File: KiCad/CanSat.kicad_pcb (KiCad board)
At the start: 4 copper layers, 50 x 55 mm, 99 parts, among them J1 GPS, J10 LED, J11 PSU_CTRL, J12 POWER, J13 SWD, J14 SDCARD, J15 DF40C-100DS-0.4V(51), J16 DF40C-100DS-0.4V(51), J17 RPI_GPIO, J2 DEPLOY, J3 TEMP, J4 ENV_SENSORS, J5 RF_DATA, J6 GND, J7 GND, J9 COMM_ANT, P1 USB_SDR, U1 Ai-Thinker-Ra-01, U2 DS18B20U+, U3 STM32F407VGTx, U4 SN74LVC1G125DCKT, U5 USBLC6-2SC6, U6 SN74LVC1G125DCKT, Y1 16M

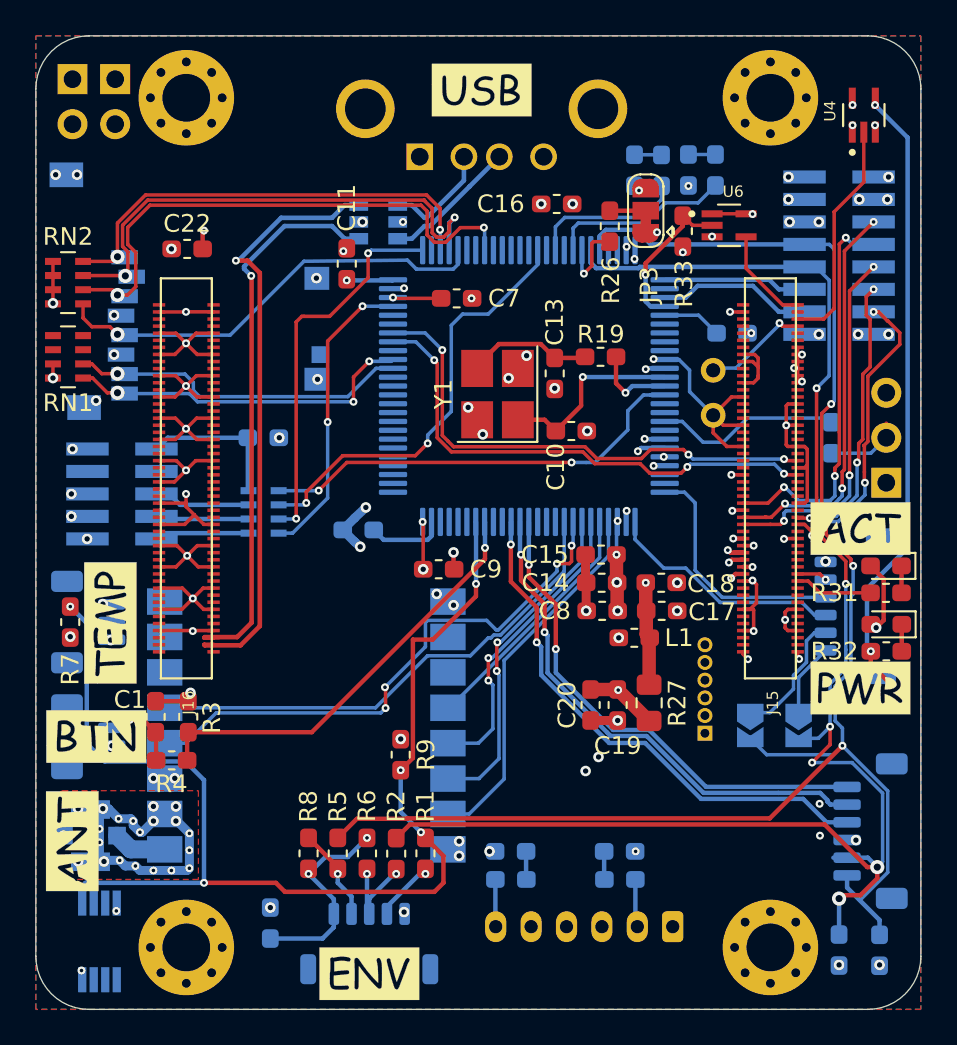
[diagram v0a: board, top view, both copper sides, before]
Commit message: Added a button and a buzzer
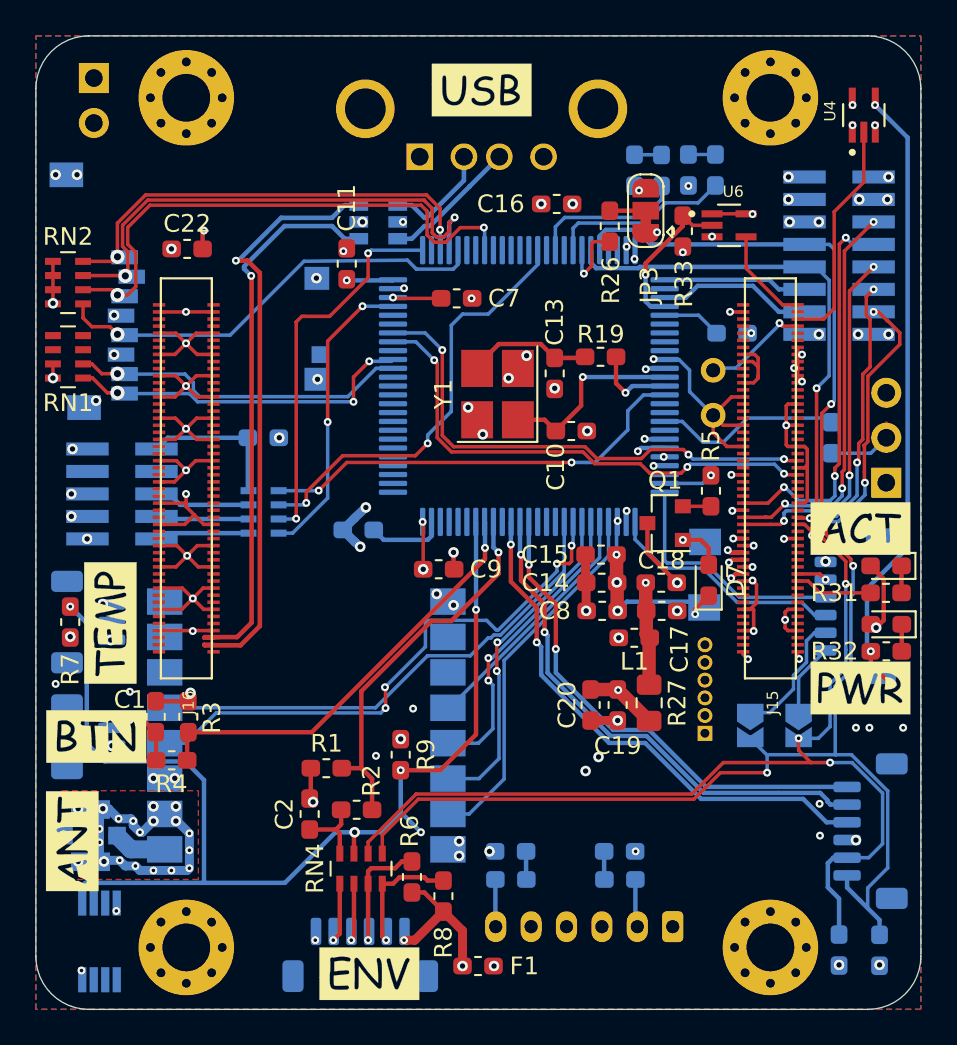
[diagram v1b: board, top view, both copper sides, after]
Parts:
- removed J7: GND, Connector_PinHeader_2.54mm:PinHeader_1x02_P2.54mm_Vertical
- added BZ1: Buzzer, Libs:MagneticBuzzer_INGHAi_GSC4417YA-16R4000, B.Cu at (222.8, 60.4)
- added C2: 1u, Capacitor_SMD:C_0603_1608Metric_Pad1.05x0.95mm_HandSolder, F.Cu at (200.5, 74.0)
- added D7: D_Small, Diode_SMD:D_0603_1608Metric_Pad1.05x0.95mm_HandSolder, F.Cu at (223.0, 60.8)
- added Q1: Q_NPN_CBE, Package_TO_SOT_SMD:SOT-23, F.Cu at (220.6, 57.5)
- added RN4: 22, Resistor_SMD:R_Array_Concave_4x0603, F.Cu at (203.4, 77.0)
- F1: moved to F.Cu
- J4: footprint Connector_JST:JST_SHL_SM05B-SHLS-TF_1x05-1MP_P1.00mm_Horizontal -> Connector_JST:JST_SH_BM06B-SRSS-TB_1x06-1MP_P1.00mm_Vertical
- R1: value 22 -> 10k
- R5: value 22 -> 1k
- moved R5 29.4 mm to (223.1, 55.7)
- moved F1 12.0 mm to (210.0, 82.5), turned to 0 degrees
- moved R8 7.99 mm to (208.0, 78.6)
- moved R1 7.38 mm to (201.4, 71.4), turned to 180 degrees
- moved R2 3.34 mm to (203.1, 73.7), turned to 0 degrees
- moved R6 2.87 mm to (206.2, 77.5), turned to 90 degrees
- moved J6 1.21 mm to (188.3, 32.4)
- moved J4 0.82 mm to (203.3, 81.9), turned to 0 degrees
- renumbered SCL to JP1, SDA to JP2, nBOOT to JP4
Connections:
- J4 pad 5: Net-(F1-Pad1) -> Net-(J4-Pad5)
- R1 pad 1: Net-(J4-Pad2) -> /Peripherals and Connectors/BUTTON
- R1 pad 2: /Peripherals and Connectors/DS_EXTERNAL -> GND
- R2 pad 1: Net-(J4-Pad3) -> Net-(C2-Pad1)
- R2 pad 2: /Peripherals and Connectors/SCL -> /Peripherals and Connectors/BUTTON
- R5 pad 1: Net-(J4-Pad4) -> Net-(Q1-Pad2)
- R5 pad 2: /Peripherals and Connectors/SDA -> /Peripherals and Connectors/BUZZER
- R6 pad 2: Net-(J4-Pad3) -> Net-(J4-Pad4)
- R8 pad 2: Net-(J4-Pad4) -> Net-(J4-Pad5)
- U3 pad 24: Net-(U3-Pad24) -> /Peripherals and Connectors/BUZZER
- U3 pad 42: Net-(U3-Pad42) -> /Peripherals and Connectors/BUTTON
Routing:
- net /Peripherals and Connectors/BUTTON: track 0.00 -> 21.6 mm, vias 0 -> 1
- net +3V3: track 277.6 -> 284.9 mm, vias 36 -> 37
- net Net-(J4-Pad5): track 0.00 -> 6.96 mm, vias 0 -> 1
- net GND: track 117.5 -> 123.3 mm, vias 98 -> 106
- net /Peripherals and Connectors/SDA: track 95.6 -> 90.1 mm
- net Net-(C2-Pad1): track 0.00 -> 4.17 mm
- net Net-(BZ1-Pad2): track 0.00 -> 3.91 mm, vias 0 -> 1
- net /Peripherals and Connectors/SCL: track 91.2 -> 87.9 mm, vias 6 -> 4
- net Net-(F1-Pad1): track 11.9 -> 8.64 mm
- net /Peripherals and Connectors/BUZZER: track 0.00 -> 2.80 mm, vias 0 -> 1
- net /Peripherals and Connectors/DS_EXTERNAL: track 68.1 -> 65.9 mm
- net Net-(J4-Pad3): track 5.28 -> 3.25 mm, vias 2 -> 1
- net Net-(Q1-Pad2): track 0.00 -> 1.59 mm
- net Net-(J4-Pad4): track 5.02 -> 6.60 mm

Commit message: Change all SH connectors to horizontal
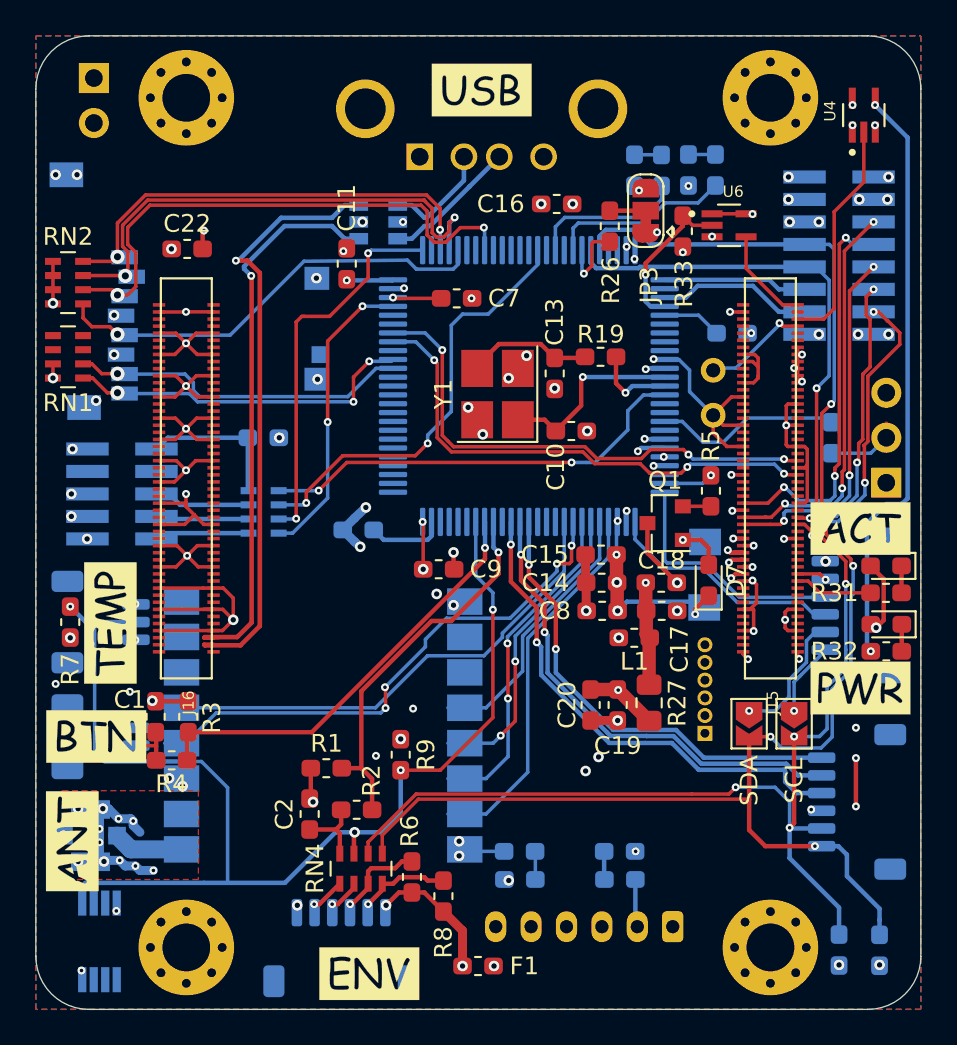
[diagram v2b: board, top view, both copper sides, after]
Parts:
- J1: footprint Connector_JST:JST_SHL_SM06B-SHLS-TF_1x06-1MP_P1.00mm_Horizontal -> Connector_JST:JST_SH_SM06B-SRSS-TB_1x06-1MP_P1.00mm_Horizontal
- J11, J4: footprint Connector_JST:JST_SH_BM06B-SRSS-TB_1x06-1MP_P1.00mm_Vertical -> Connector_JST:JST_SH_SM06B-SRSS-TB_1x06-1MP_P1.00mm_Horizontal
- J2: footprint Connector_JST:JST_SH_BM02B-SRSS-TB_1x02-1MP_P1.00mm_Vertical -> Connector_JST:JST_SH_SM02B-SRSS-TB_1x02-1MP_P1.00mm_Horizontal
- J3: footprint Connector_JST:JST_SH_BM03B-SRSS-TB_1x03-1MP_P1.00mm_Vertical -> Connector_JST:JST_SH_SM03B-SRSS-TB_1x03-1MP_P1.00mm_Horizontal
- JP1, JP2: moved to F.Cu
- JP4: value RPI_BOOT -> nBOOT
- moved G*** 3.55 mm to (226.6, 71.7)
- moved J11 1.82 mm to (231.4, 73.3), turned to 270 degrees
- moved G*** 1.16 mm to (217.9, 73.2)
- moved J4 1.15 mm to (202.2, 81.5), turned to 180 degrees
- moved U1 0.95 mm to (201.2, 69.0)
- moved J2 0.70 mm to (188.7, 69.6), turned to 90 degrees
- moved J3 0.70 mm to (188.7, 63.1), turned to 90 degrees
- moved G*** 0.52 mm to (226.9, 62.0)
- moved D2 0.51 mm to (212.3, 76.1)
- moved R12 0.51 mm to (212.3, 77.7)
- moved J1 0.31 mm to (231.6, 62.2)
- moved JP1 0.27 mm to (227.8, 68.9)
- moved G*** 0.13 mm to (216.4, 65.6)
- moved JP2 0.12 mm to (225.3, 68.9)
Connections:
- J11 pad 1: /Peripherals and Connectors/SDA -> /Power/PWR_VALID
- J11 pad 2: /Peripherals and Connectors/SCL -> /Power/PWR_WARN
- J11 pad 3: GND -> /Power/PWR_CRITICAL
- J11 pad 4: /Power/PWR_CRITICAL -> GND
- J11 pad 5: /Power/PWR_WARN -> /Peripherals and Connectors/SCL
- J11 pad 6: /Power/PWR_VALID -> /Peripherals and Connectors/SDA
- J4 pad 1: GND -> Net-(F1-Pad1)
- J4 pad 6: Net-(F1-Pad1) -> GND
- R6 pad 2: Net-(J4-Pad4) -> Net-(J4-Pad3)
- R8 pad 2: Net-(J4-Pad5) -> Net-(J4-Pad2)
- RN4 pad 1: Net-(J4-Pad2) -> Net-(J4-Pad5)
- RN4 pad 2: Net-(J4-Pad3) -> Net-(J4-Pad4)
- RN4 pad 3: Net-(J4-Pad4) -> Net-(J4-Pad3)
- RN4 pad 4: Net-(J4-Pad5) -> Net-(J4-Pad2)
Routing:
- net Net-(J4-Pad5): track 6.96 -> 1.93 mm
- net Net-(J4-Pad4): track 6.60 -> 1.85 mm
- net /Peripherals and Connectors/SCL: track 87.9 -> 84.9 mm, vias 4 -> 5
- net /Power/PWR_WARN: track 29.2 -> 26.7 mm
- net /Power/PWR_VALID: track 28.3 -> 25.8 mm
- net Net-(C1-Pad1): track 4.60 -> 2.50 mm
- net /Peripherals and Connectors/SDA: track 90.1 -> 88.2 mm, vias 3 -> 4
- net Net-(J4-Pad2): track 3.34 -> 5.17 mm
- net Net-(J4-Pad3): track 3.25 -> 5.05 mm
- net /Power/PWR_CRITICAL: track 30.1 -> 28.4 mm
- net Net-(R32-Pad2): track 34.9 -> 33.3 mm
- net /Peripherals and Connectors/DS_EXTERNAL: track 65.9 -> 67.4 mm, vias 5 -> 4
- net Net-(F1-Pad1): track 8.64 -> 7.51 mm
- net /Peripherals and Connectors/RADIO_RST: track 31.8 -> 30.7 mm
- net /Peripherals and Connectors/RADIO_MISO: track 17.2 -> 18.1 mm
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
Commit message: Dirty production PCBs commit
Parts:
- added C3: 100n, Capacitor_SMD:C_0603_1608Metric_Pad1.05x0.95mm_HandSolder, F.Cu at (201.7, 65.7)
- added C4: 100n, Capacitor_SMD:C_0603_1608Metric_Pad1.05x0.95mm_HandSolder, F.Cu at (200.8, 58.4)
- added U7: MMA8451QR1, Libs:QFN50P300X300X100-16N, F.Cu at (201.4, 62.4)
- JP4: value nBOOT -> RPI_BOOT
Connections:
- J15 pad 30: /RPi CM4/GPIO_6 -> Net-(J15-Pad30)
- J15 pad 54: Net-(J15-Pad54) -> /RPi CM4/GPIO_4
- J17 pad 5: /RPi CM4/GPIO_6 -> /RPi CM4/GPIO_5
- J17 pad 6: /RPi CM4/GPIO_5 -> /RPi CM4/GPIO_4
- U3 pad 51: Net-(U3-Pad51) -> /Peripherals and Connectors/ACC_INT2
- U3 pad 52: Net-(U3-Pad52) -> /Peripherals and Connectors/ACC_INT1
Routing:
- net /Peripherals and Connectors/SDA: track 88.2 -> 102.8 mm, vias 4 -> 6
- net /Peripherals and Connectors/SCL: track 84.9 -> 98.6 mm, vias 5 -> 7
- net /RPi CM4/GPIO_4: track 0.00 -> 11.9 mm, vias 0 -> 1
- net +3V3: track 284.0 -> 294.1 mm, vias 38 -> 41
- net /RPi CM4/GPIO_6: track 8.61 -> 0.00 mm, vias 1 -> 0
- net /Peripherals and Connectors/ACC_INT1: track 0.00 -> 8.55 mm, vias 0 -> 1
- net /Peripherals and Connectors/ACC_INT2: track 0.00 -> 7.32 mm, vias 0 -> 1
- net GND: track 123.4 -> 129.8 mm, vias 93 -> 129
- net Net-(C3-Pad1): track 0.00 -> 2.02 mm
- net /RPi CM4/GPIO_5: track 7.41 -> 8.45 mm
- net /Peripherals and Connectors/RADIO_INT: track 28.7 -> 29.1 mm, vias 0 -> 2
